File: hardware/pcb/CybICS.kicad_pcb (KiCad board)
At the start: 2 copper layers, 160 x 100 mm, 89 parts, among them J1 Raspberry_Pi_2_3, J2 Conn_01x03_Pin, J3 Conn_01x05_Pin, J4 USB_C_Receptacle_USB2.0, SW1 SW_Push, SW2 SW_Push, SW3 SW_Push, U1 STM32G070RBTx

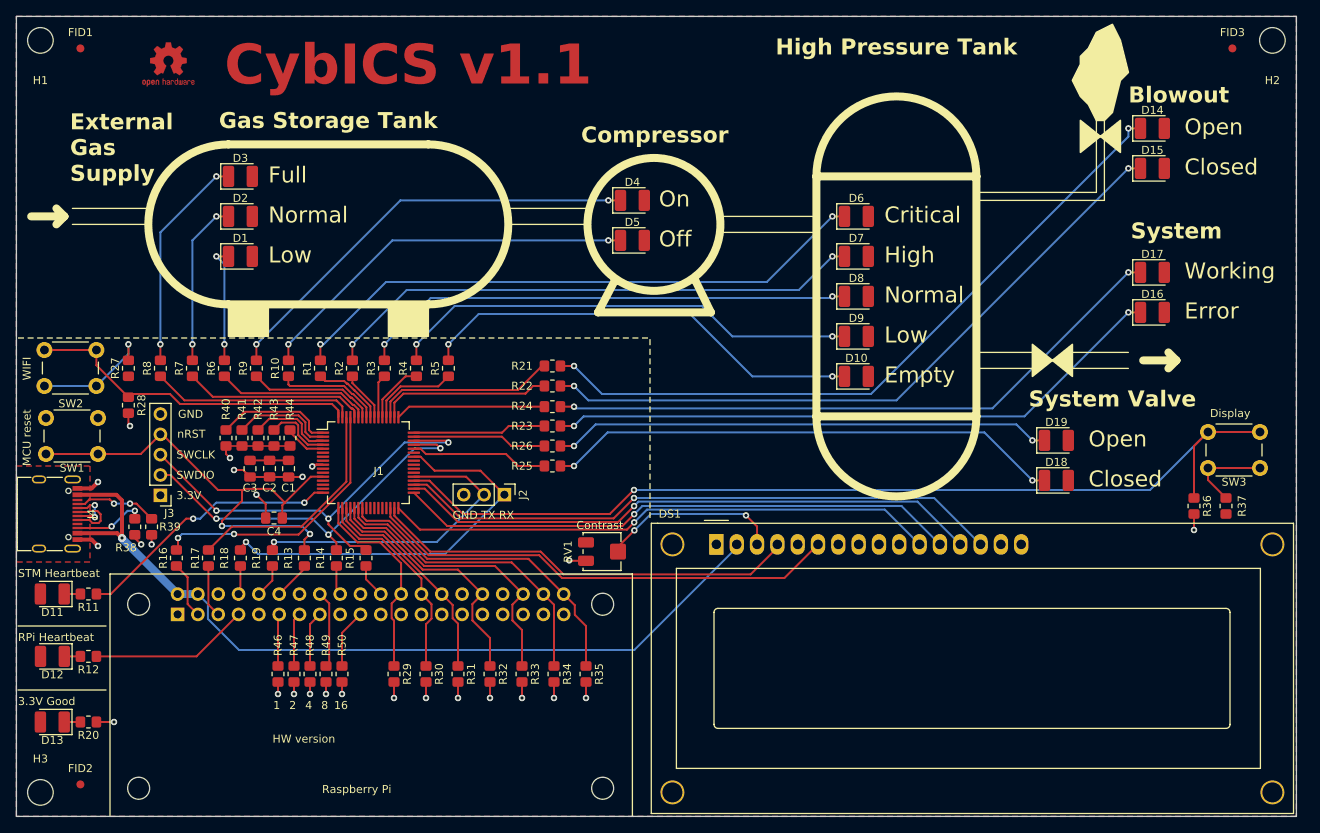
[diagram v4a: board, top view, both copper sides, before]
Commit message: fix(hardware): make the navigation switch locating holes non-plated
DRC failed with two errors, both on SW3: "Annular width ... actual
0.0000 mm" and "Padstack is questionable (PTH pad hole leaves no
copper)". The two unnamed 1.1 mm and 0.8 mm holes are the switch's
moulded locating posts, and easyeda2kicad emitted them as plated
through-holes with size equal to drill -- a plated barrel with no pad
around it, which is a manufacturing defect rather than a feature.

I had seen these when the library went in and deliberately left them as
the vendor data had them, on the reasoning that the EasyEDA footprint is
what JLCPCB assembles against. That was the wrong call: mechanical
locating posts carry no signal, so np_thru_hole is unambiguously correct,
and it is exactly what KiCad's own MountingHole footprints use -- same
size, same drill, same "*.Cu" "*.Mask" layers, only the keyword differs.

Changed in the project library and in the board's placed instance, and
only for pads whose size equals their drill, so the eight signal pads are
untouched.

Verified from hardware/pcb with kicad-cli 10.0.6: DRC at error severity
now reports 0 violations and 0 unconnected items, down from 2 errors.
Schematic parity reports 0 footprint errors, so the board matches the
schematic after the maintainer's Update PCB from Schematic and relayout.

Twelve warnings remain, all in routing and silkscreen placement, and are
reported separately rather than changed here.

Co-Authored-By: Claude Opus 5 (1M context) <noreply@anthropic.com>
Claude-Session: https://claude.ai/code/session_011zbigHZaGiZii3etPu8DwT
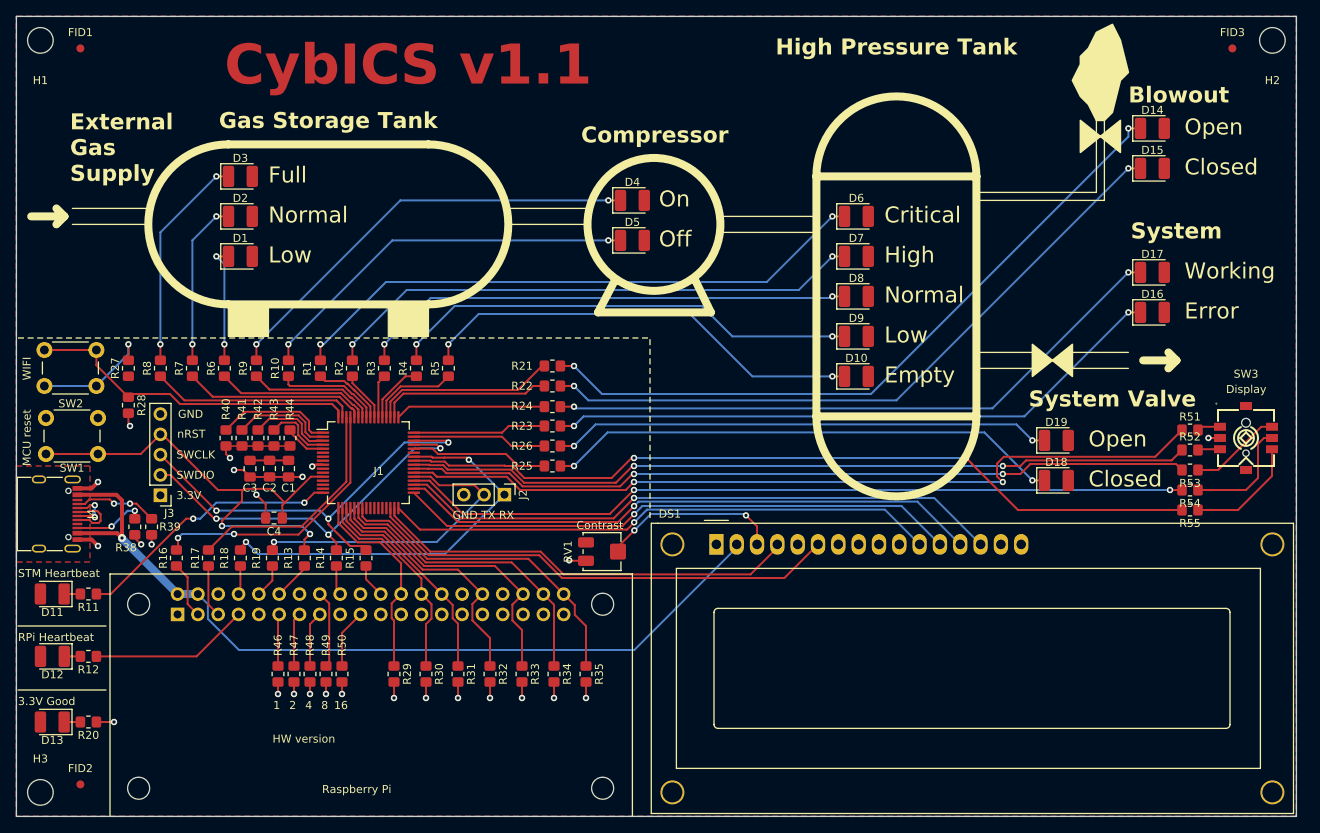
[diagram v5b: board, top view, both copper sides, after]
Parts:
- removed #SYM1: OSHW-Logo2_7.3x6mm_Copper, Symbol:OSHW-Logo2_7.3x6mm_Copper
- removed R36: 10kR, Resistor_SMD:R_0805_2012Metric_Pad1.20x1.40mm_HandSolder
- removed R37: 1kR, Resistor_SMD:R_0805_2012Metric_Pad1.20x1.40mm_HandSolder
- added R51: 1kR, Resistor_SMD:R_0805_2012Metric_Pad1.20x1.40mm_HandSolder, F.Cu at (197.5, 102.5)
- added R52: 1kR, Resistor_SMD:R_0805_2012Metric_Pad1.20x1.40mm_HandSolder, F.Cu at (197.5, 105.0)
- added R53: 1kR, Resistor_SMD:R_0805_2012Metric_Pad1.20x1.40mm_HandSolder, F.Cu at (197.5, 107.5)
- added R54: 1kR, Resistor_SMD:R_0805_2012Metric_Pad1.20x1.40mm_HandSolder, F.Cu at (197.5, 110.0)
- added R55: 1kR, Resistor_SMD:R_0805_2012Metric_Pad1.20x1.40mm_HandSolder, F.Cu at (197.5, 112.5)
- SW3: value SW_Push -> 7*7*5-6P-L WX; footprint Button_Switch_THT:SW_PUSH_6mm_H5mm -> cybics:SW-SMD_8P-L7.0-W7.0-P1.40-LS7.4-TL
- moved SW3 4.81 mm to (204.5, 103.5)
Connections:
- SW3 pad 1: /PA8 -> Net-(SW3-F2)
- SW3 pad 2: Net-(R37-Pad2) -> GND
- U1 pad 38: unconnected-(U1-PC6-Pad38) -> /NAV_F2
- U1 pad 39: unconnected-(U1-PC7-Pad39) -> /NAV_F3
- U1 pad 40: unconnected-(U1-PD8-Pad40) -> /NAV_F4
- U1 pad 41: unconnected-(U1-PD9-Pad41) -> /NAV_F5
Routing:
- net /NAV_F2: track 0.00 -> 102.4 mm, vias 0 -> 2
- net /NAV_F5: track 0.00 -> 100.7 mm, vias 0 -> 2
- net /NAV_F4: track 0.00 -> 98.8 mm, vias 0 -> 2
- net /NAV_F3: track 0.00 -> 98.4 mm, vias 0 -> 2
- net /PA8: track 120.7 -> 99.0 mm, vias 1 -> 2
- net Net-(SW3-F1): track 0.00 -> 14.4 mm
- net Net-(SW3-F5): track 0.00 -> 14.4 mm
- net Net-(SW3-F3): track 0.00 -> 12.2 mm
- net Net-(R37-Pad2): track 11.2 -> 0.00 mm
- net Net-(SW3-F2): track 0.00 -> 2.92 mm
- net Net-(SW3-F4): track 0.00 -> 2.79 mm
- net GND: track 54.5 -> 53.9 mm
- net /USART1_RX: vias 1 -> 3

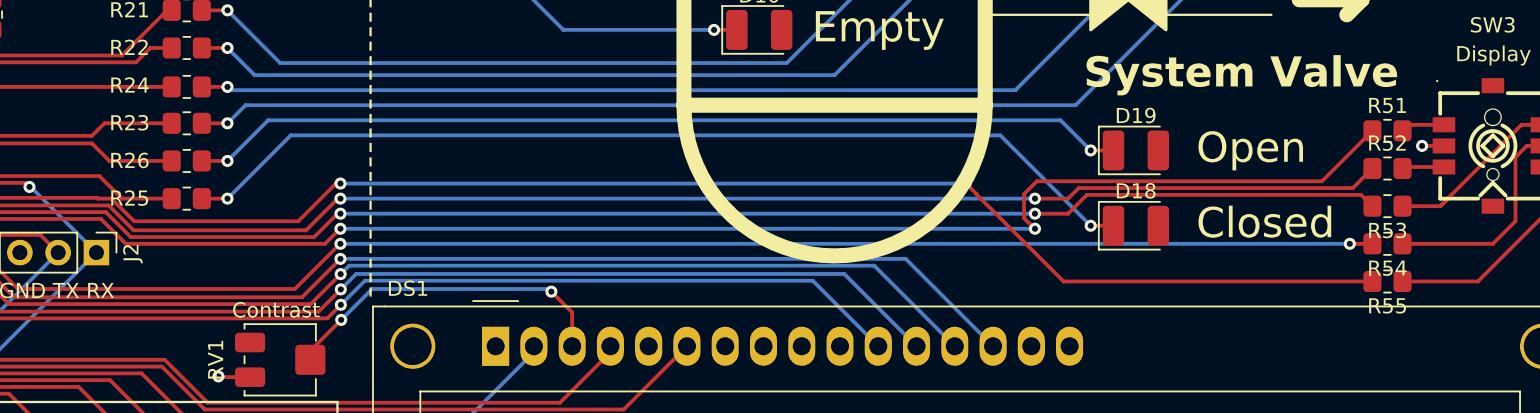
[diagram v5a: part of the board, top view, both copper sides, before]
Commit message: fix(hardware): clear the remaining DRC findings after the relayout
The relayout left twelve findings beyond the two locating-hole errors
already fixed. All of them are gone; `kicad-cli pcb drc --severity-all`
now reports 0 violations and 0 unconnected items, and KiBot's DRC job
exits 0.

  - A via sat exactly on J2 pin 1 at (111.8, 110.584). The pin is a
    plated through-hole and already bridges both layers, so the via was
    electrically redundant but put two holes at one coordinate in the
    drill file. Removed; the two B.Cu tracks still reach the pad.
  - Two track fragments with a loose end, 0.12 mm on /NAV_F4 and 0.71 mm
    on Net-(SW3-F3).
  - R51-R55 sit at 2.5 mm pitch, and the library default put each
    designator 1.65 mm from its part -- onto the neighbour's pads, where
    silkscreen is clipped in production. Moved 3.4 mm west, each label
    still beside its own resistor.
  - Update PCB from Schematic had reset the fiducial and mounting-hole
    attributes again, so FID1-FID3 were back in the position file. The
    export is 78 rows with no fiducials again. This is the third time;
    it is in CLAUDE.md and worth checking after every F8.

One change here is visible on the panel and deserves a second opinion:
the System Valve "Open" and "Closed" labels moved 2 mm west, together so
the pair stays aligned. With R51-R55 where they are, the designators of
R53 and R54 overlap "Closed" by about 1.5 mm, and no designator placement
avoids it -- east runs onto SW3's pads, smaller text falls under the
minimum silkscreen width and made things worse, and the only arrangement
that reached zero put R54's label beside R55 and R55's label below the
group, which is worse than a warning because it labels the wrong parts.
Moving the two panel labels is silkscreen-only and touches no routing.
It also brings them closer to D19 and D18, which reads better. If you
would rather move the resistor column instead, revert this one hunk.

Worth recording: KiBot fails on DRC *w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
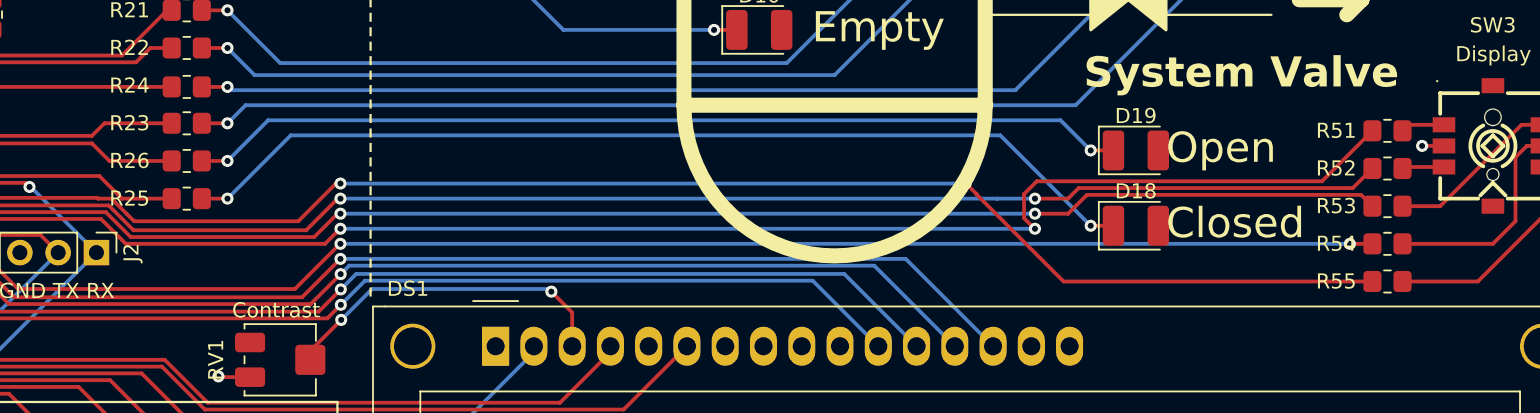
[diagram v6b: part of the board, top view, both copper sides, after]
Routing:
- net Net-(SW3-F3): track 12.2 -> 11.5 mm
- net /USART1_RX: vias 3 -> 2
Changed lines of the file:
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@@
 		(tags "resistor handsolder")
 		(property "Reference" "R55"
-			(at 0 -1.65 0)
+			(at 3.4 0 0)
 			(layer "F.SilkS")
 			(effects
@@
 			)
 		)
-		(attr smd exclude_from_bom)
+		(attr smd exclude_from_pos_files exclude_from_bom)
 		(duplicate_pad_numbers_are_jumpers no)
 		(fp_circle
@@
 		(tags "resistor handsolder")
 		(property "Reference" "R52"
-			(at 0 -1.65 0)
+			(at -3.4 0 0)
 			(layer "F.SilkS")
 			(effects
@@
 			)
 		)
-		(attr exclude_from_bom)
+		(attr exclude_from_pos_files exclude_from_bom)
 		(duplicate_pad_numbers_are_jumpers no)
 		(fp_circle
@@
 		(tags "resistor handsolder")
 		(property "Reference" "R53"
-			(at 0 -1.65 0)
+			(at 3.4 0 0)
 			(layer "F.SilkS")
 			(effects
@@
 			)
 		)
-		(attr exclude_from_bom)
+		(attr exclude_from_pos_files exclude_from_bom)
 		(duplicate_pad_numbers_are_jumpers no)
 		(fp_circle
@@
 			)
 		)
-		(attr exclude_from_bom)
+		(attr exclude_from_pos_files exclude_from_bom)
 		(duplicate_pad_numbers_are_jumpers no)
 		(fp_circle
@@
 		(tags "resistor handsolder")
 		(property "Reference" "R54"
-			(at 0 -1.65 0)
+			(at 3.4 0 0)
 			(layer "F.SilkS")
 			(effects
@@
 			)
 		)
-		(attr smd exclude_from_bom)
+		(attr smd exclude_from_pos_files exclude_from_bom)
 		(duplicate_pad_numbers_are_jumpers no)
 		(fp_circle
@@
 		(tags "resistor handsolder")
 		(property "Reference" "R51"
-			(at 0 -1.65 0)
+			(at -3.4 0 0)
 			(layer "F.SilkS")
 			(effects
@@
 			)
 		)
-		(attr smd exclude_from_bom)
+		(attr smd exclude_from_pos_files exclude_from_bom)
 		(duplicate_pad_numbers_are_jumpers no)
 		(fp_circle
@@
 	)
 	(gr_text "Open"
-		(at 184.8 104.8 0)
+		(at 182.8 104.8 0)
 		(layer "F.SilkS")
 		(effects
@@
 	)
 	(gr_text "Closed"
-		(at 184.8 109.8 0)
+		(at 182.8 109.8 0)
 		(layer "F.SilkS")
 		(effects
@@
 		(net "/USART1_RX")
 	)
-	(via
-		(at 111.8 110.584252)
-		(size 0.8)
-		(drill 0.4)
-		(layers "F.Cu" "B.Cu")
-		(net "/USART1_RX")
-	)
 	(segment
 		(start 81 118)
@@
 		(net "/NAV_F4")
 	)
-	(segment
-		(start 125.723292 109.1)
-		(end 125.6 109.1)
-		(width 0.25)
-		(layer "F.Cu")
-		(net "/NAV_F4")
-	)
 	(via
 		(at 174.1 106.999991)
@@
 		(width 0.25)
 		(layer "F.Cu")
-		(net "Net-(SW3-F3)")
-	)
-	(segment
-		(start 201 107.5)
-		(end 201.5 107)
-		(width 0.25)
-		(layer "F.Cu")
